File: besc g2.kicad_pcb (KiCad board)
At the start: 4 copper layers, 231 x 67 mm, 295 parts, among them IC1 LTC7801, J1 Phase, J10 USB_B_Micro, J11 THROTTLE, J12 MOTOR SENSOR, J13 THROTTLE 2 (BRAKE), J14 SERIAL, J15 IGNITION, J16 CAN, J17 12V OUT, J2 Phase, J3 Phase, J4 BUSBAR, J5 BUSBAR, J6 IN+, J7 IN-, J8 SWD, J9 RC PWM, Q1 Q_NMOS_DGS, Q10 Q_NMOS_DGS, Q11 Q_NMOS_DGS, Q12 Q_NMOS_DGS, Q13 Q_NMOS_DGS, Q14 Q_NMOS_DGS, Q15 Q_NMOS_DGS, Q16 Q_NMOS_DGS, Q17 Q_NMOS_DGS, Q18 Q_NMOS_DGS, Q19 Q_NMOS_DGS, Q2 Q_NMOS_DGS, Q20 Q_NMOS_DGS, Q21 Q_NMOS_DGS, Q22 Q_NMOS_DGS, Q23 Q_NMOS_DGS, Q24 Q_NMOS_DGS, Q25 FDMS86252L, Q26 BSC110N15NS5, Q3 Q_NMOS_DGS, Q4 Q_NMOS_DGS, Q5 Q_NMOS_DGS, Q6 Q_NMOS_DGS, Q7 Q_NMOS_DGS, Q8 Q_NMOS_DGS, Q9 Q_NMOS_DGS, U1 UCC21520DW, U10 TJA1051T-3, U11 R-78E5.0-0.5, U12 LP5907MFX-3.3, U2 UCC21520DW, U3 UCC21520DW, U4 INA240A1D, U5 INA240A1D, U6 INA240A1D, U7 SN74LVC1G04, U8 STM32F405RGTx, U9 USBLC6-2SC6, Y1 MCSJK-7I-8.00-18-10-60-B-10

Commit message: finished routing, added bom and step
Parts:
- added C95: 2.2u, Capacitor_SMD:C_0603_1608Metric, F.Cu at (41.8, 108.4)
- added FID1: Fiducial, Fiducial:Fiducial_0.5mm_Mask1.5mm, B.Cu at (34.5, 63.6)
- added FID2: Fiducial, Fiducial:Fiducial_0.5mm_Mask1.5mm, F.Cu at (46.8, 62.6)
- added FID3: Fiducial, Fiducial:Fiducial_0.5mm_Mask1.5mm, B.Cu at (250.8, 125.7)
- added FID4: Fiducial, Fiducial:Fiducial_0.5mm_Mask1.5mm, F.Cu at (253.3, 125.7)
- added FID5: Fiducial, Fiducial:Fiducial_0.5mm_Mask1.5mm, B.Cu at (260.6, 63.4)
- added FID6: Fiducial, Fiducial:Fiducial_0.5mm_Mask1.5mm, F.Cu at (259.6, 64.2)
- C1, C2, C3: footprint Capacitor_SMD:C_1206_3216Metric -> Capacitor_SMD:C_0805_2012Metric
- C10, C11, C12, C25, C26, C27, C28, C29, C30: footprint Capacitor_SMD:C_0805_2012Metric -> Capacitor_SMD:C_0603_1608Metric
- C100: value 4.7u -> 4.7u 25V
- C101: value 100n 50V -> 100n
- C102: value 2.2u 10V -> 2.2u
- C13, C14, C15, C4, C5, C6, C7, C8, C9: value 10n -> 270p
- C22: value 2.2u 35V -> 4.7u 25V
- C43, C46, C49, C52, C56, C57, C58, C59, C60, C61: value B41858C9477M000 -> B41858C9477M000
- C65, C66, C67: value 220p -> 270p
- C92, C93, C94, C98: footprint Capacitor_SMD:C_1206_3216Metric -> Capacitor_SMD:C_1210_3225Metric
- C99: value 4.7u -> 2.2u
- D1, D2, D3: value D_Schottky -> SS115+
- D7: value ESD 100V -> MMSZ5231BT1G
- D9: value 12.7 -> 12.7V
- FB1, FB2, FB3, FB7: value Ferrite_Bead_Small -> BLM18AG102SN1D
- FB8: value fb -> BLM18AG102SN1D
- J1, J2, J3: value Phase -> PHASE WIRE
- J10: value USB_B_Micro -> 614105150721
- Q1, Q10, Q11, Q12, Q13, Q14, Q15, Q16, Q17, Q18, Q19, Q2, Q20, Q21, Q22, Q23, Q24, Q3, Q4, Q5, Q6, Q7, Q8, Q9: value Q_NMOS_DGS -> IRF135B203
- R1, R2, R3, R4, R5, R6, R7, R8, R9: value R -> 60R4
- R10, R11, R12: value 2.2 -> 2.2R
- R13, R14, R15, R16, R17, R18, R22, R23, R24: value R -> 2k2
- R19, R20, R21: value R -> 10k
- R25, R26, R27, R28, R29, R30, R34, R35, R36, R37, R38, R39, R40, R41, R42, R43, R44, R45, R46, R47, R48, R49, R50, R51: value 10 -> 10R
- R74: value 330 -> 330R
- R75, R80: value 10k -> 2k2
- R77, R78: value 24 -> 24R
- R84, R85: value 10k -> 30k1
- R87: value 470 -> 330R
- R90: value 100k -> 80k6
- R93: footprint Resistor_SMD:R_0603_1608Metric -> Resistor_SMD:R_0805_2012Metric
- Y1: footprint Crystal:Crystal_SMD_3225-4Pin_3.2x2.5mm -> Crystal:Crystal_SMD_5032-4Pin_5.0x3.2mm
- moved C94 131.8 mm to (46.3, 120.7)
- moved C92 131.1 mm to (46.3, 117.5)
- moved C73 130.5 mm to (173.2, 118.3)
- moved Y1 130.5 mm to (169.6, 118.4), turned to 0 degrees
- moved C93 130.4 mm to (46.3, 114.2)
- moved C100 130.3 mm to (89.7, 122.4)
- moved C101 130.3 mm to (41.0, 105.4)
- moved C102 130.3 mm to (36.5, 114.9)
- moved C103 130.3 mm to (95.0, 116.4)
- moved C104 130.3 mm to (35.8, 110.2)
- moved C105 130.3 mm to (35.0, 107.7)
- moved C106 130.3 mm to (92.0, 113.4)
- moved C107 130.3 mm to (38.8, 114.2)
- moved C108 130.3 mm to (34.0, 114.2)
- moved C109 130.3 mm to (90.3, 113.4)
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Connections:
- C99 pad 1: Net-(C99-Pad1) -> GND
- C99 pad 2: GND -> /pwr mng/DRVcc
- IC1 pad 15: Net-(C99-Pad1) -> /pwr mng/DRVcc
- IC1 pad 16: Net-(C99-Pad1) -> /pwr mng/DRVcc
- J17 pad 1: +12V -> GND
- J17 pad 2: GND -> +12V
- U12 pad 4: (no net) -> +3V3
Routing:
- net /pwr mng/DRVcc: track 0.00 -> 5.26 mm, vias 0 -> 1
- net GND: track 209.2 -> 213.3 mm, vias 241 -> 242
- net Net-(C99-Pad1): track 3.47 -> 0.00 mm, vias 1 -> 0
- net /io/RX: track 61.5 -> 64.6 mm
- net Net-(C72-Pad1): track 6.53 -> 8.92 mm
- net +3V3: track 119.7 -> 121.3 mm
- net +5V: track 76.0 -> 77.0 mm
- net +12V: track 327.9 -> 328.8 mm
- net Net-(C73-Pad1): track 6.24 -> 5.37 mm
- net VDC: track 40.6 -> 40.1 mm, vias 140 -> 137
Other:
- outline, holes or cut-outs redrawn
- board text added: "!! WARNING !! Discharge capacitors before handling"
- board text added: "5V"
- board text added: "ALL VIAS MUST BE TENTED"
- board text added: "BESC Gen 2 Vinit"
- board text added: "CAN"
- board text added: "CAN_H"
- board text added: "CAN_L"
- board text added: "GND"
- board text added: "H_U"
- board text added: "H_V"
- board text added: "H_W"
- board text added: "Jul. 2019 e.pavlin.si"
- board text added: "MOTOR"
- board text added: "PPM"
- board text added: "RX"
- board text added: "SERIAL"
- board text added: "SIG"
- board text added: "THR1"
- board text added: "THR2"
- board text added: "TMP"
- board text added: "TX"

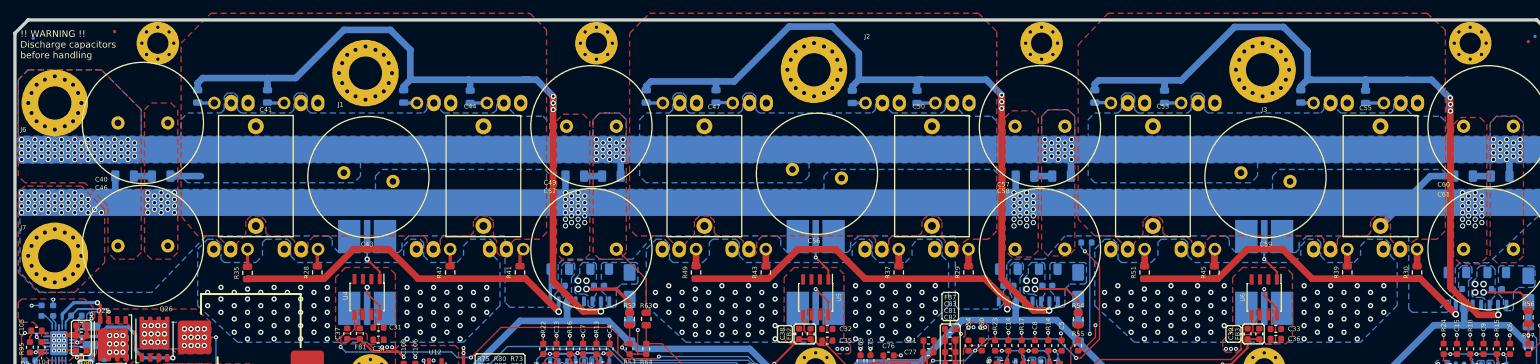
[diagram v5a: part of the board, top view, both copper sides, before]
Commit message: replaced Al capacitors with shorter ones
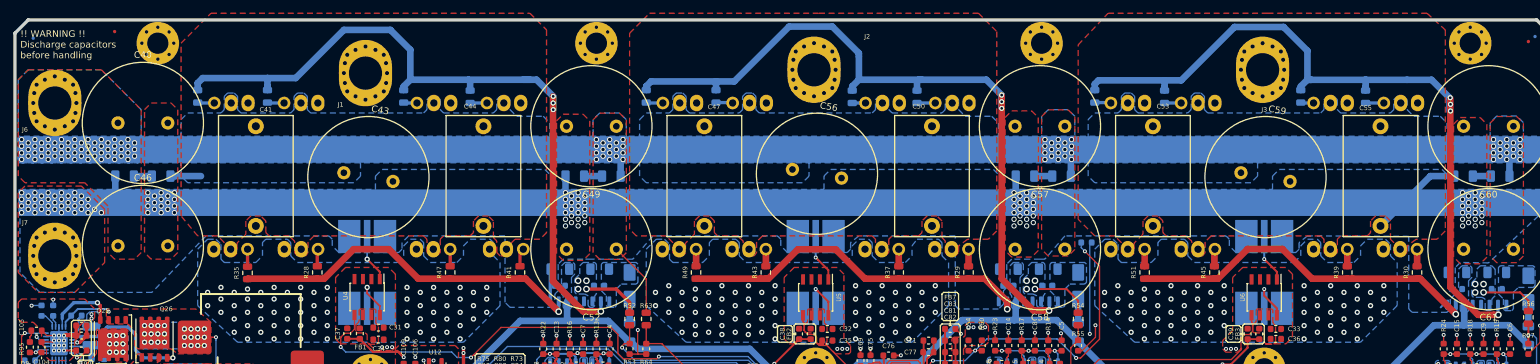
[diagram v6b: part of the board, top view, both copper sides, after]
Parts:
- C40, C43, C46, C49, C52, C56, C57, C58, C59, C60, C61: value B41858C9477M000 -> B41858D9337M000; footprint Capacitor_THT:C_Radial_D18.0mm_H35.5mm_P7.50mm -> moje:C_Radial_D18.0mm_H25mm_P7.50mm
- turned J6 to 180 degrees
- turned J7 to 180 degrees

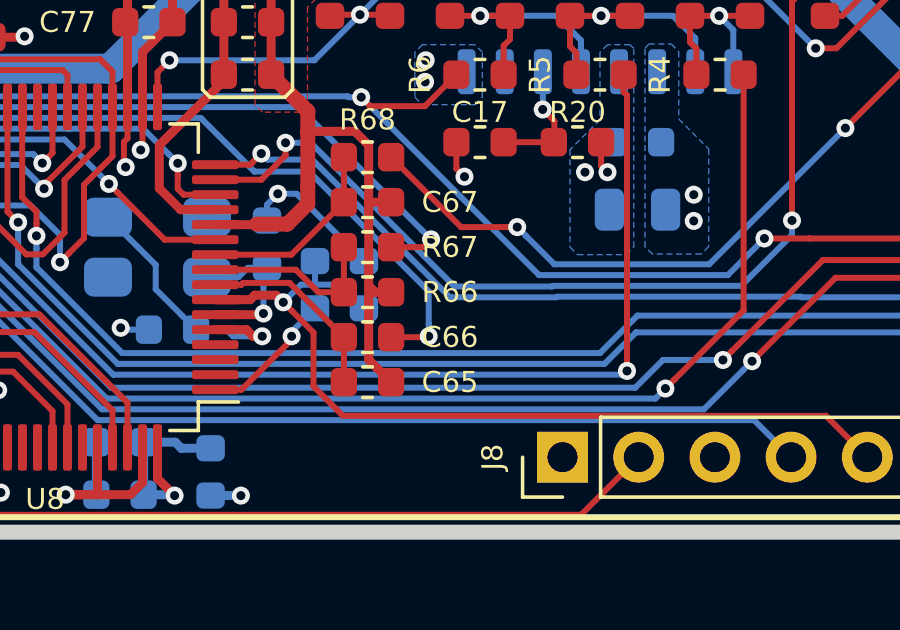
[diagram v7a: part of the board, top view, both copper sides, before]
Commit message: fixed schematic, added firmware files
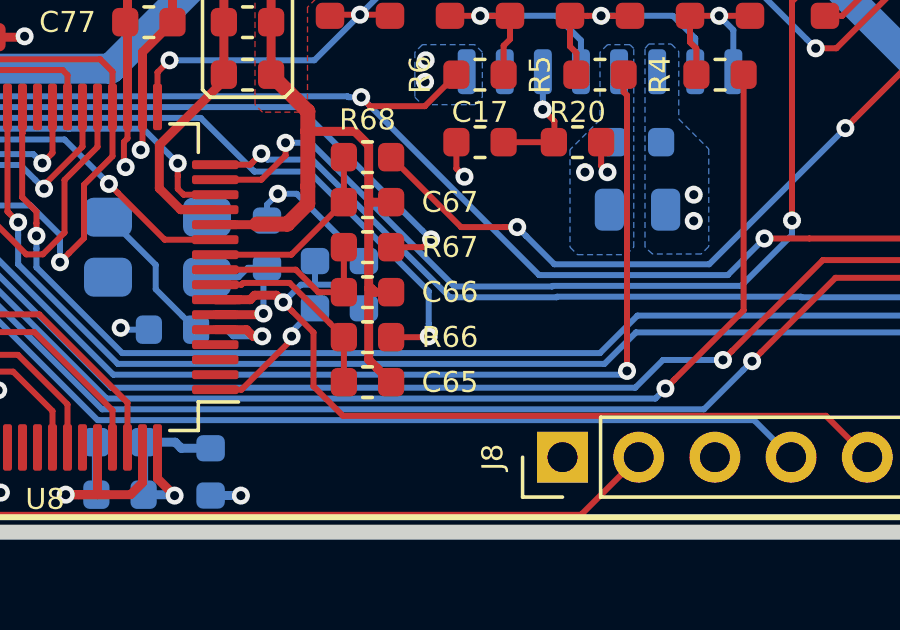
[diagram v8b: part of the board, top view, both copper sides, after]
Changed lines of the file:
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@@
   )
   (layers
-    (0 F.Cu signal hide)
+    (0 F.Cu signal)
     (1 In1.Cu signal hide)
     (2 In2.Cu signal hide)
@@
     (35 F.Paste user hide)
     (36 B.SilkS user hide)
-    (37 F.SilkS user hide)
+    (37 F.SilkS user)
     (38 B.Mask user hide)
     (39 F.Mask user hide)
@@
     (46 B.CrtYd user hide)
     (47 F.CrtYd user hide)
-    (48 B.Fab user)
-    (49 F.Fab user hide)
+    (48 B.Fab user hide)
+    (49 F.Fab user)
   )
   (setup
@@
     (tags capacitor)
     (attr smd)
-    (fp_text reference C66 (at -2.75 -1.5 180) (layer F.SilkS)
+    (fp_text reference C66 (at -2.75 0 180) (layer F.SilkS)
       (effects (font (size 0.7 0.7) (thickness 0.12)))
     )
@@
     (tags resistor)
     (attr smd)
-    (fp_text reference R66 (at 2.75 -1.5) (layer F.SilkS)
+    (fp_text reference R66 (at 2.75 0) (layer F.SilkS)
       (effects (font (size 0.7 0.7) (thickness 0.12)))
     )
